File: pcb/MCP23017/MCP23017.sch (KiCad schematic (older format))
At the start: 11 parts, among them U1 MCP23017, U2 Header2

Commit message: Added a new "power" and LEDs module (split into two half size modules)
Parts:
- HL1, HL2, HL3: symbol High-Low -> High-Low-RESCUE-MCP23017
- I1: symbol ePlayInput -> ePlayInput-RESCUE-MCP23017
- I2C1: symbol I2CHeader -> I2CHeader-RESCUE-MCP23017
- O1, O2, O3: symbol ePlayOutput -> ePlayOutput-RESCUE-MCP23017
- U2: symbol Header2 -> Header2-RESCUE-MCP23017
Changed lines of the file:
@@
 EESchema Schematic File Version 2
+LIBS:MCP23017-rescue
 LIBS:power
 LIBS:device
@@
 $EndDescr
 $Comp
-L ePlayInput I1
+L ePlayInput-RESCUE-MCP23017 I1
 U 1 1 5AC243A7
 P 1950 1600
@@
 $EndComp
 $Comp
-L ePlayOutput O1
+L ePlayOutput-RESCUE-MCP23017 O1
 U 1 1 5AC241F8
 P 6400 1600
@@
 $EndComp
 $Comp
-L ePlayOutput O3
+L ePlayOutput-RESCUE-MCP23017 O3
 U 1 1 5AC32C2A
 P 3900 5950
@@
 $EndComp
 $Comp
-L ePlayOutput O2
+L ePlayOutput-RESCUE-MCP23017 O2
 U 1 1 5AC32D5F
 P 2300 3400
@@
 GND
 $Comp
-L High-Low HL1
+L High-Low-RESCUE-MCP23017 HL1
 U 1 1 5AC332D5
 P 5550 5900
@@
 $EndComp
 $Comp
-L High-Low HL2
+L High-Low-RESCUE-MCP23017 HL2
 U 1 1 5AC33401
 P 6200 5900
@@
 $EndComp
 $Comp
-L High-Low HL3
+L High-Low-RESCUE-MCP23017 HL3
 U 1 1 5AC3345A
 P 6850 5900
@@
 VCC
 $Comp
-L I2CHeader I2C1
+L I2CHeader-RESCUE-MCP23017 I2C1
 U 1 1 5AC33E90
 P 6100 4150
@@
 GND
 $Comp
-L Header2 U2
+L Header2-RESCUE-MCP23017 U2
 U 1 1 5AC33FEE
 P 5150 4150

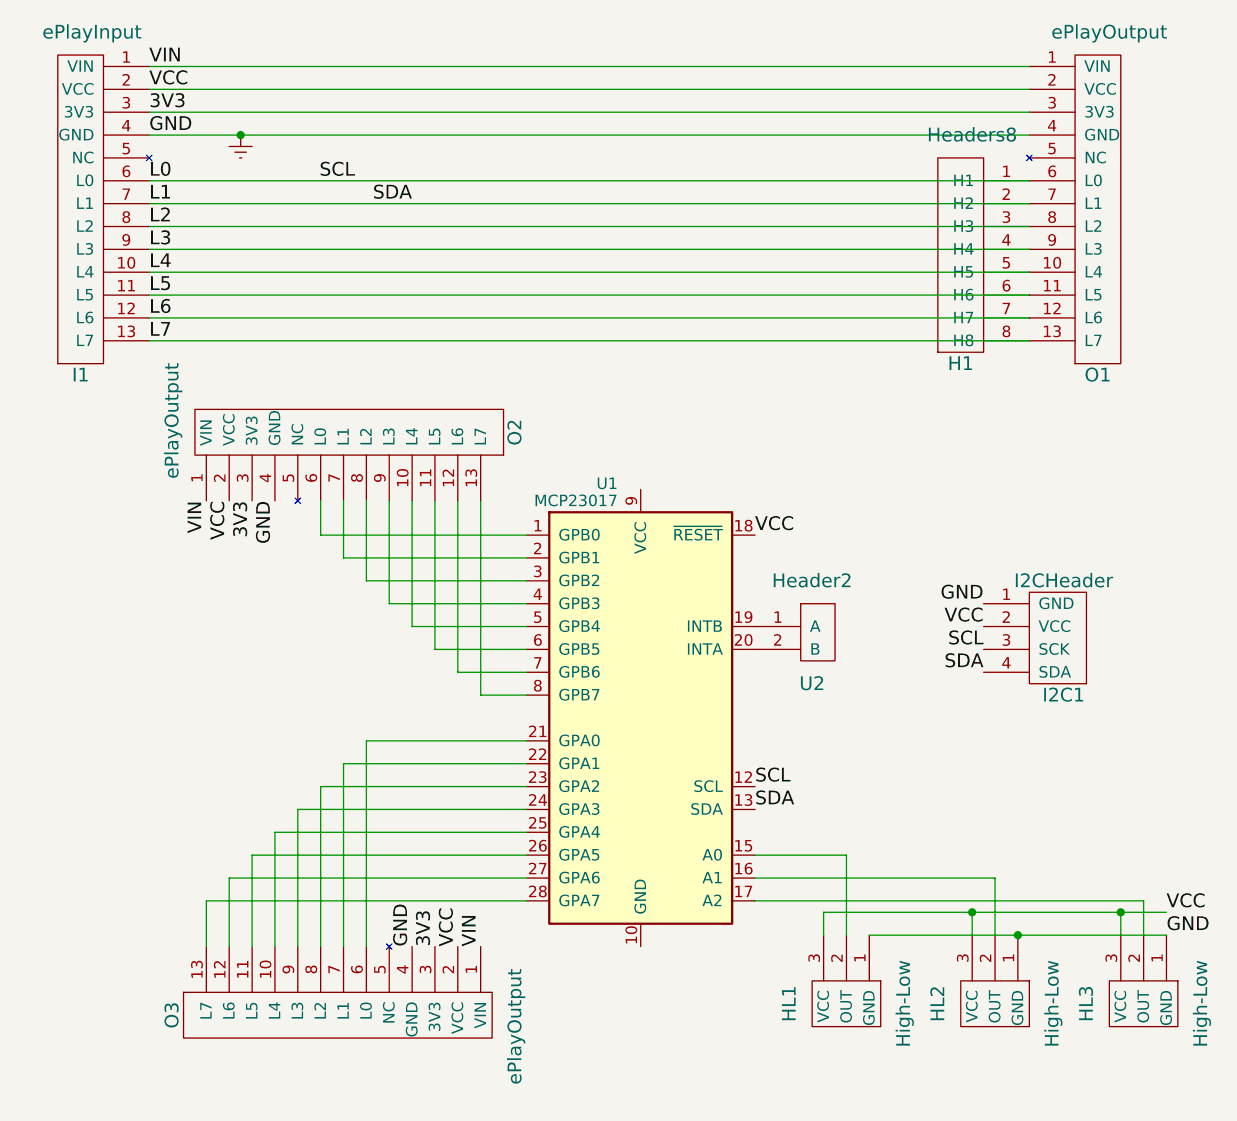
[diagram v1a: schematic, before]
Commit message: Reworked the MCP23017 I2C IO Expander module.
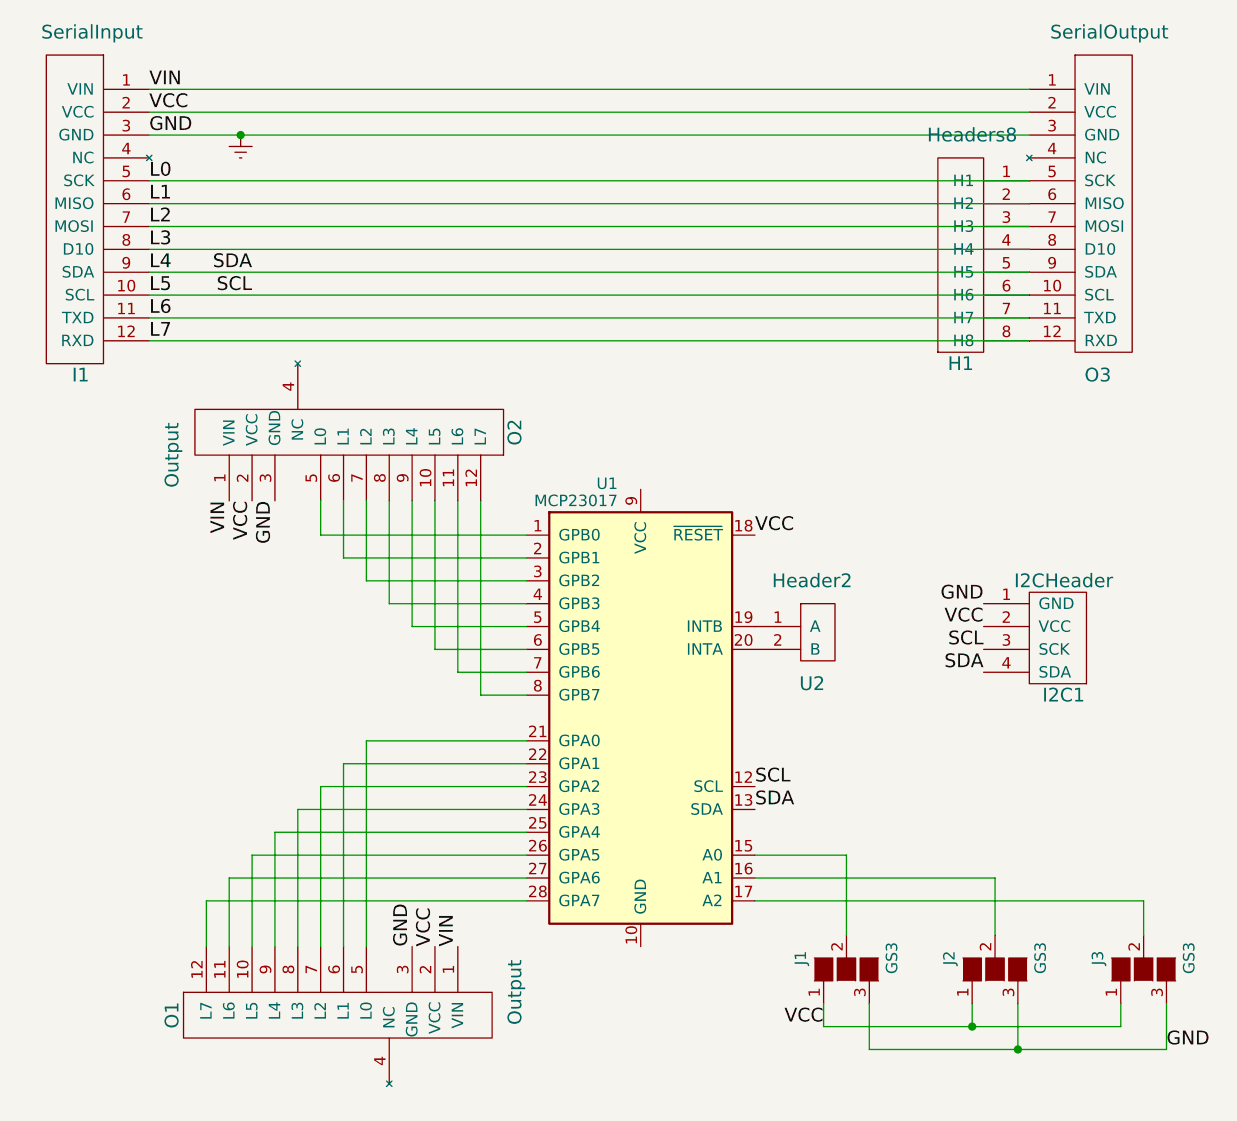
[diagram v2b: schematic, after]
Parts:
- removed HL1, HL2, HL3: High-Low, Pin_Headers:Pin_Header_Straight_1x03_Pitch2.54mm, symbol High-Low-RESCUE-MCP23017
- removed I1: ePlayInput, Pin_Headers:Pin_Header_Straight_1x13_Pitch2.54mm, symbol ePlayInput-RESCUE-MCP23017
- removed O1, O2, O3: ePlayOutput, Socket_Strips:Socket_Strip_Straight_1x13_Pitch2.54mm, symbol ePlayOutput-RESCUE-MCP23017
- added I1: SerialInput, Socket_Strips:Socket_Strip_Straight_1x12_Pitch2.54mm, symbol SerialInput
- added J1, J2, J3: GS3, Connectors:GS3, symbol GS3
- added O1, O2: Output, Socket_Strips:Socket_Strip_Straight_1x12_Pitch2.54mm, symbol Output
- added O3: SerialOutput, Socket_Strips:Socket_Strip_Straight_1x12_Pitch2.54mm, symbol SerialOutput
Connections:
- net Earth: now also I1.3 (GND), J1.3 (G3), J2.3 (G3), J3.3 (G3), O1.3 (GND), O2.3 (GND), O3.3 (GND)
- net L0: now also I1.5 (SCK), O3.5 (SCK); no longer I2C1.3 (SCK), U1.12 (SCL)
- net L1: now also I1.6 (MISO), O3.6 (MISO); no longer I2C1.4 (SDA), U1.13 (SDA)
- net L2: now also I1.7 (MOSI), O3.7 (MOSI)
- net L3: now also I1.8 (D10), O3.8 (D10)
- net L4: now also I2C1.4 (SDA), U1.13 (SDA), I1.9 (SDA), O3.9 (SDA)
- net L5: now also I2C1.3 (SCK), U1.12 (SCL), I1.10 (SCL), O3.10 (SCL)
- net L6: now also I1.11 (TXD), O3.11 (TXD)
- net L7: now also I1.12 (RXD), O3.12 (RXD)
- net VCC: now also I1.2 (VCC), J1.1 (G1), J2.1 (G1), J3.1 (G1), O1.2 (VCC), O2.2 (VCC), O3.2 (VCC)
- net VIN: now also I1.1 (VIN), O1.1 (VIN), O2.1 (VIN), O3.1 (VIN)
- net at U1.1 (GPB0): now also O2.5 (L0)
- net at U1.15 (A0): now also J1.2 (G2)
- net at U1.16 (A1): now also J2.2 (G2)
- net at U1.17 (A2): now also J3.2 (G2)
- net at U1.2 (GPB1): now also O2.6 (L1)
- net at U1.21 (GPA0): now also O1.5 (L0)
- net at U1.22 (GPA1): now also O1.6 (L1)
- net at U1.23 (GPA2): now also O1.7 (L2)
- net at U1.24 (GPA3): now also O1.8 (L3)
- net at U1.25 (GPA4): now also O1.9 (L4)
- net at U1.26 (GPA5): now also O1.10 (L5)
- net at U1.27 (GPA6): now also O1.11 (L6)
- net at U1.28 (GPA7): now also O1.12 (L7)
- net at U1.3 (GPB2): now also O2.7 (L2)
- net at U1.4 (GPB3): now also O2.8 (L3)
- net at U1.5 (GPB4): now also O2.9 (L4)
- net at U1.6 (GPB5): now also O2.10 (L5)
- net at U1.7 (GPB6): now also O2.11 (L6)
- net at U1.8 (GPB7): now also O2.12 (L7)
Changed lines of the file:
@@
 Comment4 ""
 $EndDescr
-$Comp
-L ePlayInput-RESCUE-MCP23017 I1
-U 1 1 5AC243A7
-P 1950 1600
-F 0 "I1" H 1950 50  60  0000 C CNN
-F 1 "ePlayInput" H 2000 1550 60  0000 C CNN
-F 2 "Pin_Headers:Pin_Header_Straight_1x13_Pitch2.54mm" H 2000 1550 60  0001 C CNN
-F 3 "" H 2000 1550 60  0001 C CNN
-	1    1950 1600
-	1    0    0    -1
-$EndComp
-$Comp
-L ePlayOutput-RESCUE-MCP23017 O1
-U 1 1 5AC241F8
-P 6400 1600
-F 0 "O1" H 6400 50  60  0000 C CNN
-F 1 "ePlayOutput" H 6450 1550 60  0000 C CNN
-F 2 "Socket_Strips:Socket_Strip_Straight_1x13_Pitch2.54mm" H 6450 1550 60  0001 C CNN
-F 3 "" H 6450 1550 60  0001 C CNN
-	1    6400 1600
-	1    0    0    -1
-$EndComp
 Text Label 2250 2100 0    60   ~ 0
 GND
 Text Label 2250 2000 0    60   ~ 0
-3V3
+VCC
 Text Label 2250 1900 0    60   ~ 0
-VCC
-Text Label 2250 1800 0    60   ~ 0
 VIN
 Text Label 2250 2300 0    60   ~ 0
@@
 	1    0    0    -1
 $EndComp
-$Comp
-L ePlayOutput-RESCUE-MCP23017 O3
-U 1 1 5AC32C2A
-P 3900 5950
-F 0 "O3" H 3900 4400 60  0000 C CNN
-F 1 "ePlayOutput" H 3950 5900 60  0000 C CNN
-F 2 "Socket_Strips:Socket_Strip_Straight_1x13_Pitch2.54mm" H 3950 5900 60  0001 C CNN
-F 3 "" H 3950 5900 60  0001 C CNN
-	1    3900 5950
-	0    1    1    0
-$EndComp
-$Comp
-L ePlayOutput-RESCUE-MCP23017 O2
-U 1 1 5AC32D5F
-P 2300 3400
-F 0 "O2" H 2300 1850 60  0000 C CNN
-F 1 "ePlayOutput" H 2350 3350 60  0000 C CNN
-F 2 "Socket_Strips:Socket_Strip_Straight_1x13_Pitch2.54mm" H 2350 3350 60  0001 C CNN
-F 3 "" H 2350 3350 60  0001 C CNN
-	1    2300 3400
-	0    -1   -1   0
-$EndComp
-Text Label 2500 3700 3    60   ~ 0
+Text Label 2600 3700 3    60   ~ 0
 VIN
-Text Label 2600 3700 3    60   ~ 0
-VCC
 Text Label 2700 3700 3    60   ~ 0
-3V3
+VCC
 Text Label 2800 3700 3    60   ~ 0
 GND
-Text Label 3700 5650 1    60   ~ 0
+Text Label 3600 5650 1    60   ~ 0
 VIN
-Text Label 3600 5650 1    60   ~ 0
-VCC
 Text Label 3500 5650 1    60   ~ 0
-3V3
+VCC
 Text Label 3400 5650 1    60   ~ 0
 GND
-$Comp
-L High-Low-RESCUE-MCP23017 HL1
-U 1 1 5AC332D5
-P 5550 5900
-F 0 "HL1" H 5550 5400 60  0000 C CNN
-F 1 "High-Low" H 5550 5900 60  0000 C CNN
-F 2 "Pin_Headers:Pin_Header_Straight_1x03_Pitch2.54mm" H 5550 5900 60  0001 C CNN
-F 3 "" H 5550 5900 60  0001 C CNN
-	1    5550 5900
-	0    1    1    0
-$EndComp
-$Comp
-L High-Low-RESCUE-MCP23017 HL2
-U 1 1 5AC33401
-P 6200 5900
-F 0 "HL2" H 6200 5400 60  0000 C CNN
-F 1 "High-Low" H 6200 5900 60  0000 C CNN
-F 2 "Pin_Headers:Pin_Header_Straight_1x03_Pitch2.54mm" H 6200 5900 60  0001 C CNN
-F 3 "" H 6200 5900 60  0001 C CNN
-	1    6200 5900
-	0    1    1    0
-$EndComp
-$Comp
-L High-Low-RESCUE-MCP23017 HL3
-U 1 1 5AC3345A
-P 6850 5900
-F 0 "HL3" H 6850 5400 60  0000 C CNN
-F 1 "High-Low" H 6850 5900 60  0000 C CNN
-F 2 "Pin_Headers:Pin_Header_Straight_1x03_Pitch2.54mm" H 6850 5900 60  0001 C CNN
-F 3 "" H 6850 5900 60  0001 C CNN
-	1    6850 5900
-	0    1    1    0
-$EndComp
-Wire Wire Line
-	2250 1800 6100 1800
 Wire Wire Line
 	2250 1900 6100 1900
@@
 Wire Wire Line
 	6600 5450 6600 5600
-Wire Wire Line
-	5200 5600 5200 5500
-Wire Wire Line
-	5200 5500 6700 5500
-Wire Wire Line
-	5850 5500 5850 5600
-Wire Wire Line
-	6500 5500 6500 5600
-Connection ~ 5850 5500
-Wire Wire Line
-	5400 5600 6700 5600
-Connection ~ 6050 5600
-Connection ~ 6500 5500
-Text Label 6700 5500 0    60   ~ 0
-VCC
-Text Label 6700 5600 0    60   ~ 0
-GND
-Text Label 3150 2300 2    60   ~ 0
+Text Label 5200 6000 2    60   ~ 0
+VCC
+Text Label 6700 6100 0    60   ~ 0
+GND
+Text Label 2700 2800 2    60   ~ 0
 SCL
-Text Label 3400 2400 2    60   ~ 0
+Text Label 2700 2700 2    60   ~ 0
 SDA
 Text Label 4900 5050 0    60   ~ 0
@@
 	1    0    0    -1
 $EndComp
+$Comp
+L GS3 J1
+U 1 1 5AC7B0E5
+P 5300 5750
+F 0 "J1" H 5350 5950 50  0000 C CNN
+F 1 "GS3" H 5350 5551 50  0000 C CNN
+F 2 "Connectors:GS3" V 5388 5676 50  0001 C CNN
+F 3 "" H 5300 5750 50  0001 C CNN
+	1    5300 5750
+	0    -1   -1   0
+$EndComp
+$Comp
+L GS3 J2
+U 1 1 5AC7B1FC
+P 5950 5750
+F 0 "J2" H 6000 5950 50  0000 C CNN
+F 1 "GS3" H 6000 5551 50  0000 C CNN
+F 2 "Connectors:GS3" V 6038 5676 50  0001 C CNN
+F 3 "" H 5950 5750 50  0001 C CNN
+	1    5950 5750
+	0    -1   -1   0
+$EndComp
+$Comp
+L GS3 J3
+U 1 1 5AC7B231
+P 6600 5750
+F 0 "J3" H 6650 5950 50  0000 C CNN
+F 1 "GS3" H 6650 5551 50  0000 C CNN
+F 2 "Connectors:GS3" V 6688 5676 50  0001 C CNN
+F 3 "" H 6600 5750 50  0001 C CNN
+	1    6600 5750
+	0    -1   -1   0
+$EndComp
+Wire Wire Line
+	5200 5900 5200 6000
+Wire Wire Line
+	5200 6000 6500 6000
+Wire Wire Line
+	5850 6000 5850 5900
+Wire Wire Line
+	6500 6000 6500 5900
+Connection ~ 5850 6000
+Wire Wire Line
+	5400 5900 5400 6100
+Wire Wire Line
+	5400 6100 6700 6100
+Wire Wire Line
+	6050 6100 6050 5900
+Wire Wire Line
+	6700 6100 6700 5900
+Connection ~ 6050 6100
+$Comp
+L Output O1
+U 1 1 5AC7B49B
+P 3900 5950
+F 0 "O1" H 3900 4400 60  0000 C CNN
+F 1 "Output" H 3800 5900 60  0000 C CNN
+F 2 "Socket_Strips:Socket_Strip_Straight_1x12_Pitch2.54mm" H 3950 5900 60  0001 C CNN
+F 3 "" H 3950 5900 60  0001 C CNN
+	1    3900 5950
+	0    1    1    0
+$EndComp
+$Comp
+L Output O2
+U 1 1 5AC7BA28
+P 2300 3400
+F 0 "O2" H 2300 1850 60  0000 C CNN
+F 1 "Output" H 2200 3350 60  0000 C CNN
+F 2 "Socket_Strips:Socket_Strip_Straight_1x12_Pitch2.54mm" H 2350 3350 60  0001 C CNN
+F 3 "" H 2350 3350 60  0001 C CNN
+	1    2300 3400
+	0    -1   -1   0
+$EndComp
+$Comp
+L SerialOutput O3
+U 1 1 5AC7BD75
+P 6400 1600
+F 0 "O3" H 6400 50  60  0000 C CNN
+F 1 "SerialOutput" H 6450 1550 60  0000 C CNN
+F 2 "Socket_Strips:Socket_Strip_Straight_1x12_Pitch2.54mm" H 6450 1550 60  0001 C CNN
+F 3 "" H 6450 1550 60  0001 C CNN
+	1    6400 1600
+	1    0    0    -1
+$EndComp
+$Comp
+L SerialInput I1
+U 1 1 5AC7BF99
+P 1950 1600
+F 0 "I1" H 1950 50  60  0000 C CNN
+F 1 "SerialInput" H 2000 1550 60  0000 C CNN
+F 2 "Socket_Strips:Socket_Strip_Straight_1x12_Pitch2.54mm" H 2000 1550 60  0001 C CNN
+F 3 "" H 2000 1550 60  0001 C CNN
+	1    1950 1600
+	1    0    0    -1
+$EndComp

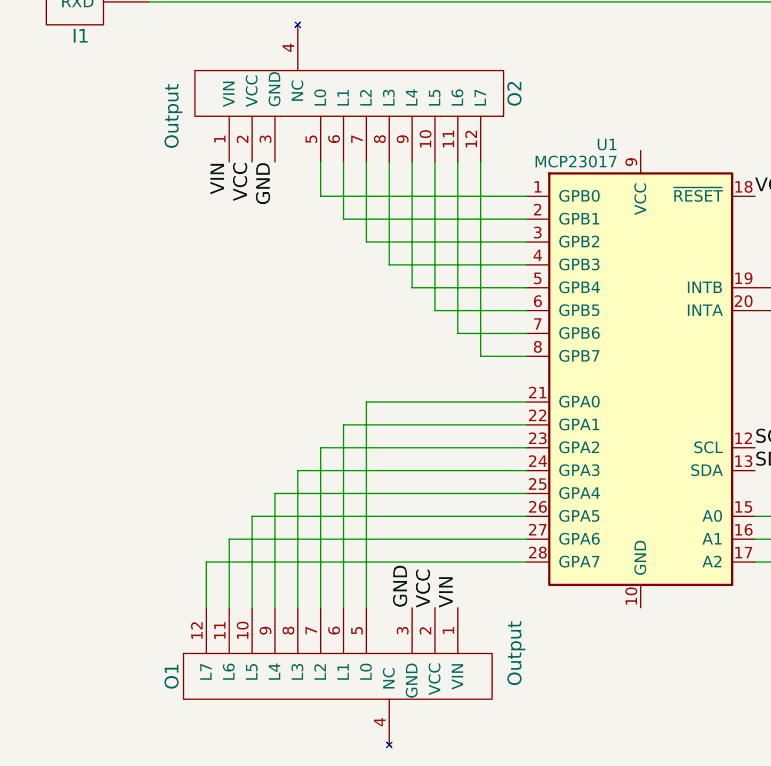
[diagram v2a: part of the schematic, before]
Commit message: Added a multiplexer module (which works in master and slave mode, for up to 40:1 with 5 boards)
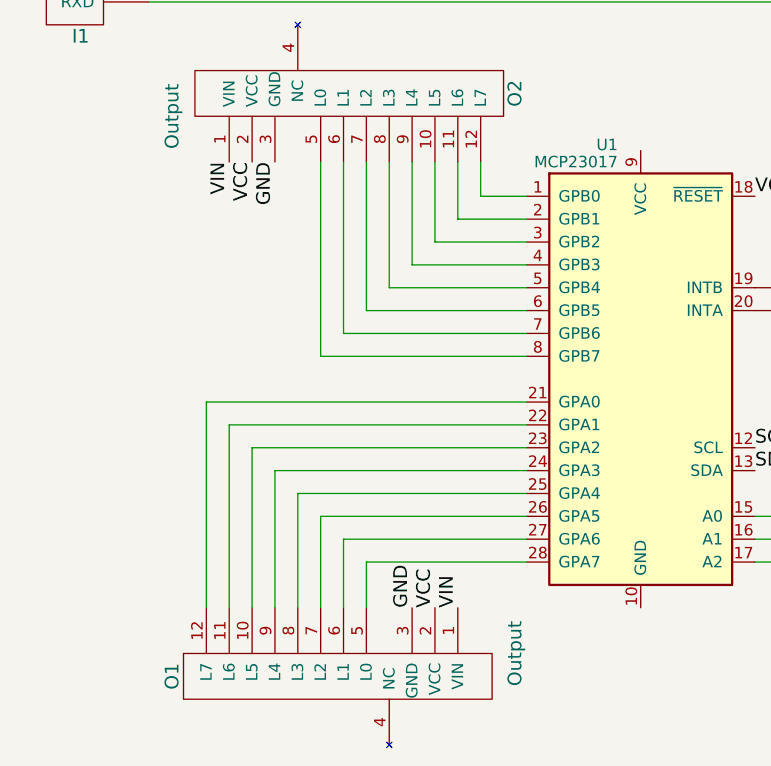
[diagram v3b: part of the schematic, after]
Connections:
- net at U1.1 (GPB0): now also O2.12 (L7); no longer O2.5 (L0)
- net at U1.2 (GPB1): now also O2.11 (L6); no longer O2.6 (L1)
- net at U1.21 (GPA0): now also O1.12 (L7); no longer O1.5 (L0)
- net at U1.22 (GPA1): now also O1.11 (L6); no longer O1.6 (L1)
- net at U1.23 (GPA2): now also O1.10 (L5); no longer O1.7 (L2)
- net at U1.24 (GPA3): now also O1.9 (L4); no longer O1.8 (L3)
- net at U1.25 (GPA4): now also O1.8 (L3); no longer O1.9 (L4)
- net at U1.26 (GPA5): now also O1.7 (L2); no longer O1.10 (L5)
- net at U1.27 (GPA6): now also O1.6 (L1); no longer O1.11 (L6)
- net at U1.28 (GPA7): now also O1.5 (L0); no longer O1.12 (L7)
- net at U1.3 (GPB2): now also O2.10 (L5); no longer O2.7 (L2)
- net at U1.4 (GPB3): now also O2.9 (L4); no longer O2.8 (L3)
- net at U1.5 (GPB4): now also O2.8 (L3); no longer O2.9 (L4)
- net at U1.6 (GPB5): now also O2.7 (L2); no longer O2.10 (L5)
- net at U1.7 (GPB6): now also O2.6 (L1); no longer O2.11 (L6)
- net at U1.8 (GPB7): now also O2.5 (L0); no longer O2.12 (L7)
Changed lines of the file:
@@
 Connection ~ 2650 2100
-Wire Wire Line
-	3000 3700 3000 3850
-Wire Wire Line
-	3000 3850 3900 3850
-Wire Wire Line
-	3900 3950 3100 3950
-Wire Wire Line
-	3100 3950 3100 3700
-Wire Wire Line
-	3200 3700 3200 4050
-Wire Wire Line
-	3200 4050 3900 4050
-Wire Wire Line
-	3300 3700 3300 4150
-Wire Wire Line
-	3300 4150 3900 4150
-Wire Wire Line
-	3400 3700 3400 4250
-Wire Wire Line
-	3400 4250 3900 4250
-Wire Wire Line
-	3500 3700 3500 4350
-Wire Wire Line
-	3500 4350 3900 4350
-Wire Wire Line
-	3600 3700 3600 4450
-Wire Wire Line
-	3600 4450 3900 4450
-Wire Wire Line
-	3700 3700 3700 4550
-Wire Wire Line
-	3700 4550 3900 4550
-Wire Wire Line
-	3900 4750 3200 4750
-Wire Wire Line
-	3200 4750 3200 5650
-Wire Wire Line
-	3900 4850 3100 4850
-Wire Wire Line
-	3100 4850 3100 5650
-Wire Wire Line
-	3900 4950 3000 4950
-Wire Wire Line
-	3000 4950 3000 5650
-Wire Wire Line
-	3900 5050 2900 5050
-Wire Wire Line
-	2900 5050 2900 5650
-Wire Wire Line
-	3900 5150 2800 5150
-Wire Wire Line
-	2800 5150 2800 5650
-Wire Wire Line
-	3900 5250 2700 5250
-Wire Wire Line
-	2700 5250 2700 5650
-Wire Wire Line
-	3900 5350 2600 5350
-Wire Wire Line
-	2600 5350 2600 5650
-Wire Wire Line
-	3900 5450 2500 5450
-Wire Wire Line
-	2500 5450 2500 5650
 Wire Wire Line
 	4900 5250 5300 5250
@@
 	1    0    0    -1
 $EndComp
+Wire Wire Line
+	3000 4550 3900 4550
+Wire Wire Line
+	3000 4550 3000 3700
+Wire Wire Line
+	3100 3700 3100 4450
+Wire Wire Line
+	3100 4450 3900 4450
+Wire Wire Line
+	3200 3700 3200 4350
+Wire Wire Line
+	3200 4350 3900 4350
+Wire Wire Line
+	3300 3700 3300 4250
+Wire Wire Line
+	3300 4250 3900 4250
+Wire Wire Line
+	3900 4150 3400 4150
+Wire Wire Line
+	3400 4150 3400 3700
+Wire Wire Line
+	3500 3700 3500 4050
+Wire Wire Line
+	3500 4050 3900 4050
+Wire Wire Line
+	3900 3950 3600 3950
+Wire Wire Line
+	3600 3950 3600 3700
+Wire Wire Line
+	3700 3700 3700 3850
+Wire Wire Line
+	3700 3850 3900 3850
+Wire Wire Line
+	3200 5650 3200 5450
+Wire Wire Line
+	3200 5450 3900 5450
+Wire Wire Line
+	3900 5350 3100 5350
+Wire Wire Line
+	3100 5350 3100 5650
+Wire Wire Line
+	3000 5250 3000 5650
+Wire Wire Line
+	3000 5250 3900 5250
+Wire Wire Line
+	3900 5150 2900 5150
+Wire Wire Line
+	2900 5150 2900 5650
+Wire Wire Line
+	2800 5650 2800 5050
+Wire Wire Line
+	2800 5050 3900 5050
+Wire Wire Line
+	3900 4950 2700 4950
+Wire Wire Line
+	2700 4950 2700 5650
+Wire Wire Line
+	2600 5650 2600 4850
+Wire Wire Line
+	2600 4850 3900 4850
+Wire Wire Line
+	3900 4750 2500 4750
+Wire Wire Line
+	2500 4750 2500 5650
 $EndSCHEMATC
